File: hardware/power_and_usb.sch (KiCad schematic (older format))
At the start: 17 parts

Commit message: Finished routing USB type-c and battery charging IC
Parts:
- added C?: 10uF 25V, symbol Device:C
- added C?: 4.7uF, symbol Device:C
- added C?: 47nF, symbol Device:C
- added C? (x2): 10uF, symbol Device:C
- added C?: 8.2uF, symbol Device:C
- added C?: 1uF, symbol Device:C
- added C? (x2): 100nF, symbol Device:C
- added D?: LED, symbol Device:LED
- added JP?: Jumper, symbol Jumper:Jumper_2_Open
- added L?: 1uF, symbol Device:L
- added Q?: SN7002NH6327, Package_TO_SOT_SMD:SOT-23, symbol Device:Q_NMOS_GDS
- added R? (x2): 5K1, symbol Device:R
- added R?: 2K2, symbol Device:R
- added R?: 260R, symbol Device:R
- added R?: 5.23K, symbol Device:R
- added R?: 30.1K, symbol Device:R
- added R? (x6): 10K, symbol Device:R
- added R? (x2): 0R, Resistor_SMD:R_1206_3216Metric, symbol Device:R
- added R?: 220R, symbol Device:R
- added TH?: Thermistor 10k, symbol Device:Thermistor
- BT?: value Battery_Cell -> Li-Po Battery; Battery Description (none) -> 1S 3.7V 5000mAh
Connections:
- net labels added: BQ25890_INT, BQ25890_SCL, BQ25890_SDA, CE, CH340_RX, CH340_TX, DC-DC_PWR, GNDREF, Q_BOOST, Q_DISABLE, REGN, USB_PWR_D+, VBUS
- wire segments 45 -> 109
- no-connect marks 0 -> 13
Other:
- note added: "3.5...4.5V"
- note added: "3.9...14V at 3A"
- note added: "Solder it after programming and debugging"
- note added: "With/Without battery selector"
- note added: "with\nbattery"
- note added: "without\nbattery"
- note removed: "???"
- note removed: "Solder it after everything"
- moved on the sheet: BT?

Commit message: Add cubemx project Changed MCU and PD scheme
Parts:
- removed BT?: Li-Po Battery, symbol Device:Battery_Cell
- removed C?: 10uF 25V, symbol Device:C
- removed C?: 4.7uF, symbol Device:C
- removed C?: 47nF, symbol Device:C
- removed C? (x2): 10uF, symbol Device:C
- removed C?: 8.2uF, symbol Device:C
- removed C?: 1uF, symbol Device:C
- removed C?: 100nF, symbol Device:C
- removed D?: LED, symbol Device:LED
- removed JP?: Jumper, symbol Jumper:Jumper_2_Open
- removed L?: 1uF, symbol Device:L
- removed Q?: SN7002NH6327, Package_TO_SOT_SMD:SOT-23, symbol Device:Q_NMOS_GDS
- removed R? (x2): 5K1, symbol Device:R
- removed R?: 2K2, symbol Device:R
- removed R?: 260R, symbol Device:R
- removed R?: 5.23K, symbol Device:R
- removed R?: 30.1K, symbol Device:R
- removed R? (x6): 10K, symbol Device:R
- removed R?: 220R, symbol Device:R
- removed TH?: Thermistor 10k, symbol Device:Thermistor
- removed U?: BQ25890RTWR, QFN50P400X400X80-25N, symbol Batery:BQ25890RTWR
- added C?: 0.1uF, symbol Device:C
- added R?: 330R, symbol Device:R
- added U?: FUSB302BMPX, Package_DFN_QFN:WQFN-14-1EP_2.5x2.5mm_P0.5mm_EP1.45x1.45mm, symbol Interface_USB:FUSB302BMPX
- added U?: TPD4E02B04DQA, Package_SON:USON-10_2.5x1.0mm_P0.5mm, symbol Power_Protection:TPD4E02B04DQA
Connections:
- net labels added: CC1, CC2
- net labels removed: BQ25890_INT, BQ25890_SCL, BQ25890_SDA, CE, GNDREF, Q_BOOST, Q_DISABLE, REGN
- wire segments 109 -> 60
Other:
- note added: "ESD protection"
- note removed: "3.5...4.5V"
- note removed: "3.9...14V at 3A"
- moved on the sheet: J?, R?

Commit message: Changed flash for esp8266 Added stm32 schematic
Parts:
- removed C?: 100nF, symbol Device:C
- removed U?: CH340E, Package_SO:MSOP-10_3x3mm_P0.5mm, symbol Interface_USB:CH340E
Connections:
- net labels removed: CH340_RX, CH340_TX
- wire segments 60 -> 59
- no-connect marks 13 -> 10
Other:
- note removed: "USB-UART"
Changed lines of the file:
@@
 	4500 1150 5050 1150
-$Comp
-L Interface_USB:CH340E U?
-U 1 1 603B0049
-P 6450 5450
-F 0 "U?" H 6200 6000 50  0000 C CNN
-F 1 "CH340E" H 6650 4850 50  0000 C CNN
-F 2 "Package_SO:MSOP-10_3x3mm_P0.5mm" H 6500 4900 50  0001 L CNN
-F 3 "https://www.mpja.com/download/35227cpdata.pdf" H 6100 6250 50  0001 C CNN
-	1    6450 5450
-	1    0    0    -1
-$EndComp
-$Comp
-L power:GND #PWR?
-U 1 1 603B004F
-P 6450 6050
-F 0 "#PWR?" H 6450 5800 50  0001 C CNN
-F 1 "GND" H 6455 5877 50  0000 C CNN
-F 2 "" H 6450 6050 50  0001 C CNN
-F 3 "" H 6450 6050 50  0001 C CNN
-	1    6450 6050
-	1    0    0    -1
-$EndComp
-Text Notes 5950 6050 0    50   ~ 0
-USB-UART
 $Comp
 L Type-C:105450-0101 J?
@@
 Wire Notes Line
 	-700 5850 -2700 5850
-Text Label 6050 5450 2    50   ~ 0
-USB_UART_D-
-Text Label 6050 5350 2    50   ~ 0
-USB_UART_D+
 NoConn ~ 1050 7100
 NoConn ~ 1050 7000
@@
 Wire Notes Line
 	-700 3800 -2700 3800
-$Comp
-L power:+3.3V #PWR?
-U 1 1 6052E7D8
-P 6350 4850
-F 0 "#PWR?" H 6350 4700 50  0001 C CNN
-F 1 "+3.3V" H 6365 5023 50  0000 C CNN
-F 2 "" H 6350 4850 50  0001 C CNN
-F 3 "" H 6350 4850 50  0001 C CNN
-	1    6350 4850
-	1    0    0    -1
-$EndComp
-Wire Wire Line
-	6450 4850 6350 4850
-Connection ~ 6350 4850
-Text HLabel 6850 5050 2    50   Output ~ 0
-CH340_TX
-Text HLabel 6850 5150 2    50   Input ~ 0
-CH340_RX
-NoConn ~ 6850 5850
-NoConn ~ 6850 5350
-NoConn ~ 6050 5550
 Text Label 4300 2000 0    50   ~ 0
 DC-DC_PWR
-$Comp
-L Device:C C?
-U 1 1 6053E82B
-P 7300 5650
-F 0 "C?" H 7415 5696 50  0000 L CNN
-F 1 "100nF" H 7415 5605 50  0000 L CNN
-F 2 "" H 7338 5500 50  0001 C CNN
-F 3 "~" H 7300 5650 50  0001 C CNN
-	1    7300 5650
-	1    0    0    -1
-$EndComp
-$Comp
-L power:+3.3V #PWR?
-U 1 1 605408B8
-P 7300 5500
-F 0 "#PWR?" H 7300 5350 50  0001 C CNN
-F 1 "+3.3V" H 7315 5673 50  0000 C CNN
-F 2 "" H 7300 5500 50  0001 C CNN
-F 3 "" H 7300 5500 50  0001 C CNN
-	1    7300 5500
-	1    0    0    -1
-$EndComp
-$Comp
-L power:GND #PWR?
-U 1 1 6054128D
-P 7300 5800
-F 0 "#PWR?" H 7300 5550 50  0001 C CNN
-F 1 "GND" H 7305 5627 50  0000 C CNN
-F 2 "" H 7300 5800 50  0001 C CNN
-F 3 "" H 7300 5800 50  0001 C CNN
-	1    7300 5800
-	1    0    0    -1
-$EndComp
 Text Notes -3950 4050 0    50   ~ 0
 without\nbattery

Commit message: Changing power circuit again
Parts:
- removed JP? (x2): Jumper, symbol Jumper:Jumper_3_Open
- removed R? (x2): 0R, symbol Device:R
- removed R? (x2): 0R, Resistor_SMD:R_1206_3216Metric, symbol Device:R
- removed U?: FUSB302BMPX, Package_DFN_QFN:WQFN-14-1EP_2.5x2.5mm_P0.5mm_EP1.45x1.45mm, symbol Interface_USB:FUSB302BMPX
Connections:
- net labels removed: USB_PWR_D+, USB_PWR_D-, USB_UART_D+, USB_UART_D-, VCC
- wire segments 59 -> 54
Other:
- note removed: "Solder it after programming and debugging"
- note removed: "Use it during programming"
- note removed: "With/Without battery selector"
- note removed: "do NOT use BOTH top and bottom schematics"
- note removed: "with\nbattery"
- note removed: "without\nbattery"
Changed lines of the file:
@@
 Text Notes 1250 7500 0    50   ~ 0
 Type-C header
-$Comp
-L Jumper:Jumper_3_Open JP?
-U 1 1 603B9872
-P -2400 4350
-F 0 "JP?" V -2446 4437 50  0000 L CNN
-F 1 "Jumper" V -2355 4437 50  0000 L CNN
-F 2 "" H -2400 4350 50  0001 C CNN
-F 3 "~" H -2400 4350 50  0001 C CNN
-	1    -2400 4350
-	0    1    1    0
-$EndComp
-$Comp
-L Jumper:Jumper_3_Open JP?
-U 1 1 603BC5B8
-P -1500 4350
-F 0 "JP?" V -1546 4437 50  0000 L CNN
-F 1 "Jumper" V -1455 4437 50  0000 L CNN
-F 2 "" H -1500 4350 50  0001 C CNN
-F 3 "~" H -1500 4350 50  0001 C CNN
-	1    -1500 4350
-	0    1    1    0
-$EndComp
 Text Label 2450 6600 0    50   ~ 0
 D+
@@
 Text Label 2450 6700 0    50   ~ 0
 D-
-Text Label -2550 4350 0    50   ~ 0
-D+
-Text Label -1650 4350 0    50   ~ 0
-D-
-Text Label -2400 4100 0    50   ~ 0
-USB_UART_D+
-Text Label -1500 4100 0    50   ~ 0
-USB_UART_D-
-Text Label -1400 4600 0    50   ~ 0
-USB_PWR_D-
-Text Label -2300 4600 0    50   ~ 0
-USB_PWR_D+
-Wire Wire Line
-	-1500 4600 -1400 4600
-Wire Wire Line
-	-2400 4600 -2300 4600
-$Comp
-L Device:R R?
-U 1 1 603C2BE1
-P -1950 5200
-F 0 "R?" V -2157 5200 50  0000 C CNN
-F 1 "0R" V -2066 5200 50  0000 C CNN
-F 2 "" V -2020 5200 50  0001 C CNN
-F 3 "~" H -1950 5200 50  0001 C CNN
-	1    -1950 5200
-	0    1    1    0
-$EndComp
-$Comp
-L Device:R R?
-U 1 1 603C3C5A
-P -1950 5600
-F 0 "R?" V -2157 5600 50  0000 C CNN
-F 1 "0R" V -2066 5600 50  0000 C CNN
-F 2 "" V -2020 5600 50  0001 C CNN
-F 3 "~" H -1950 5600 50  0001 C CNN
-	1    -1950 5600
-	0    1    1    0
-$EndComp
-Text Label -1800 5200 0    50   ~ 0
-USB_PWR_D+
-Text Label -1800 5600 0    50   ~ 0
-USB_PWR_D-
-Text Label -2100 5600 2    50   ~ 0
-D-
-Text Label -2100 5200 2    50   ~ 0
-D+
-Wire Notes Line
-	-2600 4700 -850 4700
-Wire Notes Line
-	-850 4700 -850 4000
-Wire Notes Line
-	-850 4000 -2600 4000
-Wire Notes Line
-	-2600 4000 -2600 4700
-Wire Notes Line
-	-2250 4950 -2250 5700
-Wire Notes Line
-	-2250 5700 -1250 5700
-Wire Notes Line
-	-1250 5700 -1250 4950
-Wire Notes Line
-	-1250 4950 -2250 4950
-Text Notes -2250 3950 0    50   ~ 0
-Use it during programming
-Text Notes -2550 5800 0    50   ~ 0
-Solder it after programming and debugging
-Text Notes -2650 4850 0    50   ~ 0
-do NOT use BOTH top and bottom schematics
-Wire Notes Line
-	-2700 5850 -2700 3800
-Wire Notes Line
-	-700 5850 -2700 5850
 NoConn ~ 1050 7100
 NoConn ~ 1050 7000
@@
 Text Label 700  850  0    50   ~ 0
 DC-DC_PWR
-$Comp
-L Device:R R?
-U 1 1 6045FB2F
-P -4100 4150
-F 0 "R?" V -4307 4150 50  0000 C CNN
-F 1 "0R" V -4216 4150 50  0000 C CNN
-F 2 "Resistor_SMD:R_1206_3216Metric" V -4170 4150 50  0001 C CNN
-F 3 "~" H -4100 4150 50  0001 C CNN
-	1    -4100 4150
-	0    1    1    0
-$EndComp
-$Comp
-L Device:R R?
-U 1 1 604601EF
-P -4100 4550
-F 0 "R?" V -4307 4550 50  0000 C CNN
-F 1 "0R" V -4216 4550 50  0000 C CNN
-F 2 "Resistor_SMD:R_1206_3216Metric" V -4170 4550 50  0001 C CNN
-F 3 "~" H -4100 4550 50  0001 C CNN
-	1    -4100 4550
-	0    1    1    0
-$EndComp
-Text Label -3950 4150 0    50   ~ 0
-DC-DC_PWR
-Text Label -3950 4550 0    50   ~ 0
-DC-DC_PWR
-$Comp
-L power:VBUS #PWR?
-U 1 1 60465C61
-P -4400 4150
-F 0 "#PWR?" H -4400 4000 50  0001 C CNN
-F 1 "VBUS" H -4385 4323 50  0000 C CNN
-F 2 "" H -4400 4150 50  0001 C CNN
-F 3 "" H -4400 4150 50  0001 C CNN
-	1    -4400 4150
-	1    0    0    -1
-$EndComp
-$Comp
-L power:VCC #PWR?
-U 1 1 60466B91
-P -4400 4550
-F 0 "#PWR?" H -4400 4400 50  0001 C CNN
-F 1 "VCC" H -4385 4723 50  0000 C CNN
-F 2 "" H -4400 4550 50  0001 C CNN
-F 3 "" H -4400 4550 50  0001 C CNN
-	1    -4400 4550
-	1    0    0    -1
-$EndComp
-Wire Wire Line
-	-4400 4550 -4250 4550
-Wire Wire Line
-	-4400 4150 -4250 4150
-Wire Notes Line
-	-4550 4650 -3450 4650
-Wire Notes Line
-	-3450 4650 -3450 3850
-Wire Notes Line
-	-3450 3850 -4550 3850
-Wire Notes Line
-	-4550 3850 -4550 4650
-Text Notes -4550 3800 0    50   ~ 0
-With/Without battery selector
-Wire Notes Line
-	-700 5850 -700 3800
-Wire Notes Line
-	-700 3800 -2700 3800
 Text Label 4300 2000 0    50   ~ 0
 DC-DC_PWR
-Text Notes -3950 4050 0    50   ~ 0
-without\nbattery
-Text Notes -3950 4450 0    50   ~ 0
-with\nbattery
-$Comp
-L power:VBUS #PWR?
-U 1 1 603EA1A9
-P 9900 5450
-F 0 "#PWR?" H 9900 5300 50  0001 C CNN
-F 1 "VBUS" H 9915 5623 50  0000 C CNN
-F 2 "" H 9900 5450 50  0001 C CNN
-F 3 "" H 9900 5450 50  0001 C CNN
-	1    9900 5450
-	1    0    0    -1
-$EndComp
-Wire Wire Line
-	9900 5450 9800 5450
-$Comp
-L Interface_USB:FUSB302BMPX U?
-U 1 1 603EFB15
-P 9300 5550
-F 0 "U?" H 9300 5061 50  0000 C CNN
-F 1 "FUSB302BMPX" H 9300 4970 50  0000 C CNN
-F 2 "Package_DFN_QFN:WQFN-14-1EP_2.5x2.5mm_P0.5mm_EP1.45x1.45mm" H 9300 5050 50  0001 C CNN
-F 3 "http://www.onsemi.com/pub/Collateral/FUSB302B-D.PDF" H 9400 5150 50  0001 C CNN
-	1    9300 5550
-	1    0    0    -1
-$EndComp
 Text Label 1050 6400 2    50   ~ 0
 CC2

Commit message: Finished power schematics
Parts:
- removed C?: 10uF 25V, symbol Device:C
- removed C?: 3.3nF, symbol Device:C
- removed C?: 100nF, symbol Device:C
- removed C?: 22uF, symbol Device:C
- removed L?: 2.2uH, symbol Device:L
- removed R? (x2): 100K, symbol Device:R
- removed R?: 316K, symbol Device:R
- removed U?: TPS62150RGTR, QFN50P300X300X100-17N, symbol TSP62150:TPS62150RGTR
- added BT?: Li-Po Battery, symbol Device:Battery_Cell
- added C? (x3): 100nF, symbol Device:C
- added C?: 10uF 25V, symbol Device:C
- added C?: 4.7uF, symbol Device:C
- added C?: 47nF, symbol Device:C
- added C? (x3): 10uF, symbol Device:C
- added C? (x4): 1uF, symbol Device:C
- added C? (x2): 470pF, symbol Device:C
- added D?: TS3USB221DCDR, Package_SON:VSON-10-1EP_3x3mm_P0.5mm_EP1.65x2.4mm_ThermalVias, symbol ts3usb221dcdr:TS3USB221DCDR
- added D?: LED, symbol Device:LED
- added L?: 2.2uH, symbol Device:L
- added R? (x4): 4K7, symbol Device:R
- added R?: 2K2, symbol Device:R
- added R?: 260R, symbol Device:R
- added R?: 5K23, symbol Device:R
- added R?: 30K1, symbol Device:R
- added R? (x5): 10K, symbol Device:R
- added R? (x3): 0R, symbol Device:R
- added R? (x2): 5K1, symbol Device:R
- added R?: 200R, symbol Device:R
- added SW?: Button, symbol Switch:SW_Push
- added TH?: Thermistor 10K, symbol Device:Thermistor
- added U?: BQ25895RTW, Package_DFN_QFN:Texas_S-PWQFN-N24_EP2.7x2.7mm_ThermalVias, symbol Battery_Management:BQ25895RTW
- added U?: TLV75533PDBV, Package_TO_SOT_SMD:SOT-23-5, symbol Regulator_Linear:TLV75533PDBV
- added U?: FUSB302BMPX, Package_DFN_QFN:WQFN-14-1EP_2.5x2.5mm_P0.5mm_EP1.45x1.45mm, symbol Interface_USB:FUSB302BMPX
- C?: value 0.1uF -> 100nF
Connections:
- net labels added: BQ25895_INT, BQ25895_SCL, BQ25895_SDA, ChargeEnable, ControlSelect, FUSB302_INT, FUSB302_SCL, FUSB302_SDA, GNDA, GNDPWR, USB_D+, USB_D-, USB_PWR_D+, USB_PWR_D-, VCC
- net labels removed: DC-DC_PWR, FB, VOS
- wire segments 54 -> 127
- no-connect marks 10 -> 11
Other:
- note added: "+5V"
- note added: "3.5...4.75V"
- note added: "3.9...14V at 3A"
- note added: "500mA"
- note added: "Battery Thermistor"
- note added: "Full reset"
- note added: "If without battery, place R \ninstead of TS3USB221"
- note added: "If without battery,\nplace R \ninstead of FUSB302"
- note added: "WITHOUT\nBATTERY\nJUMPER"
- note added: "Without battery:\n- no bq25895\n- no fusb302mpx, R on CC pins instead\n- TLV75533 jumper\n"
- note removed: "3.3...17V"
- note removed: "AVIN - AGND\ncapacitor"
- moved on the sheet: C?, J?, R?, U?

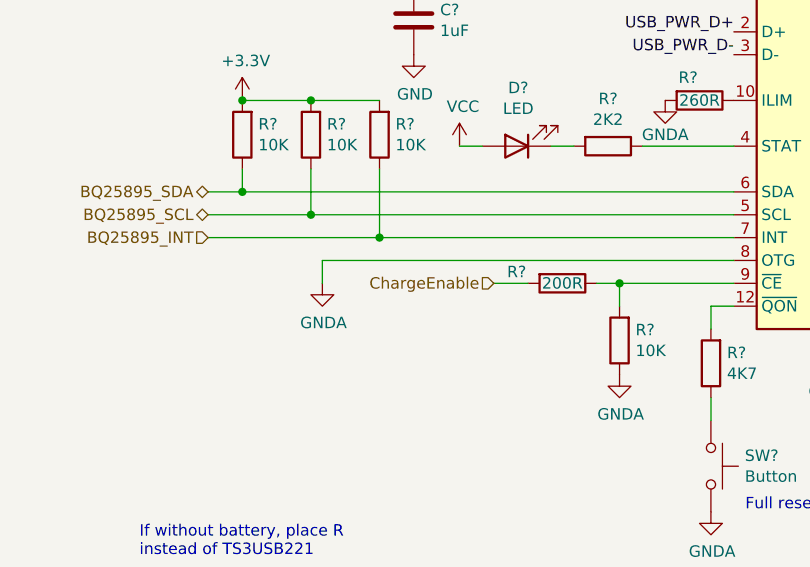
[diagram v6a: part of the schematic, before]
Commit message: Finished sx1278 schematic
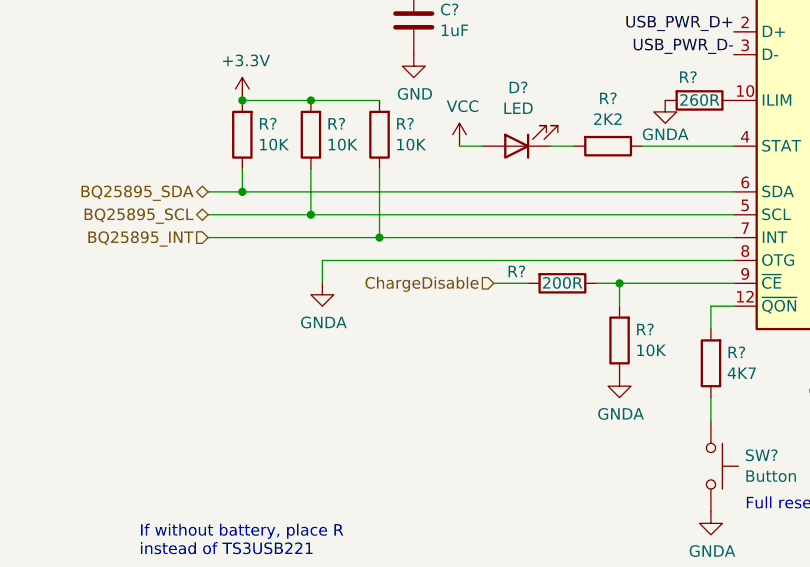
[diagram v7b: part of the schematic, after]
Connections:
- net ChargeEnable renamed ChargeDisable
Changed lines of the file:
@@
 	8100 3500 8850 3500
 Text HLabel 6250 4600 0    50   Input ~ 0
-ChargeEnable
+ChargeDisable
 Text Label 8500 4400 0    50   ~ 0
 ControlSelect

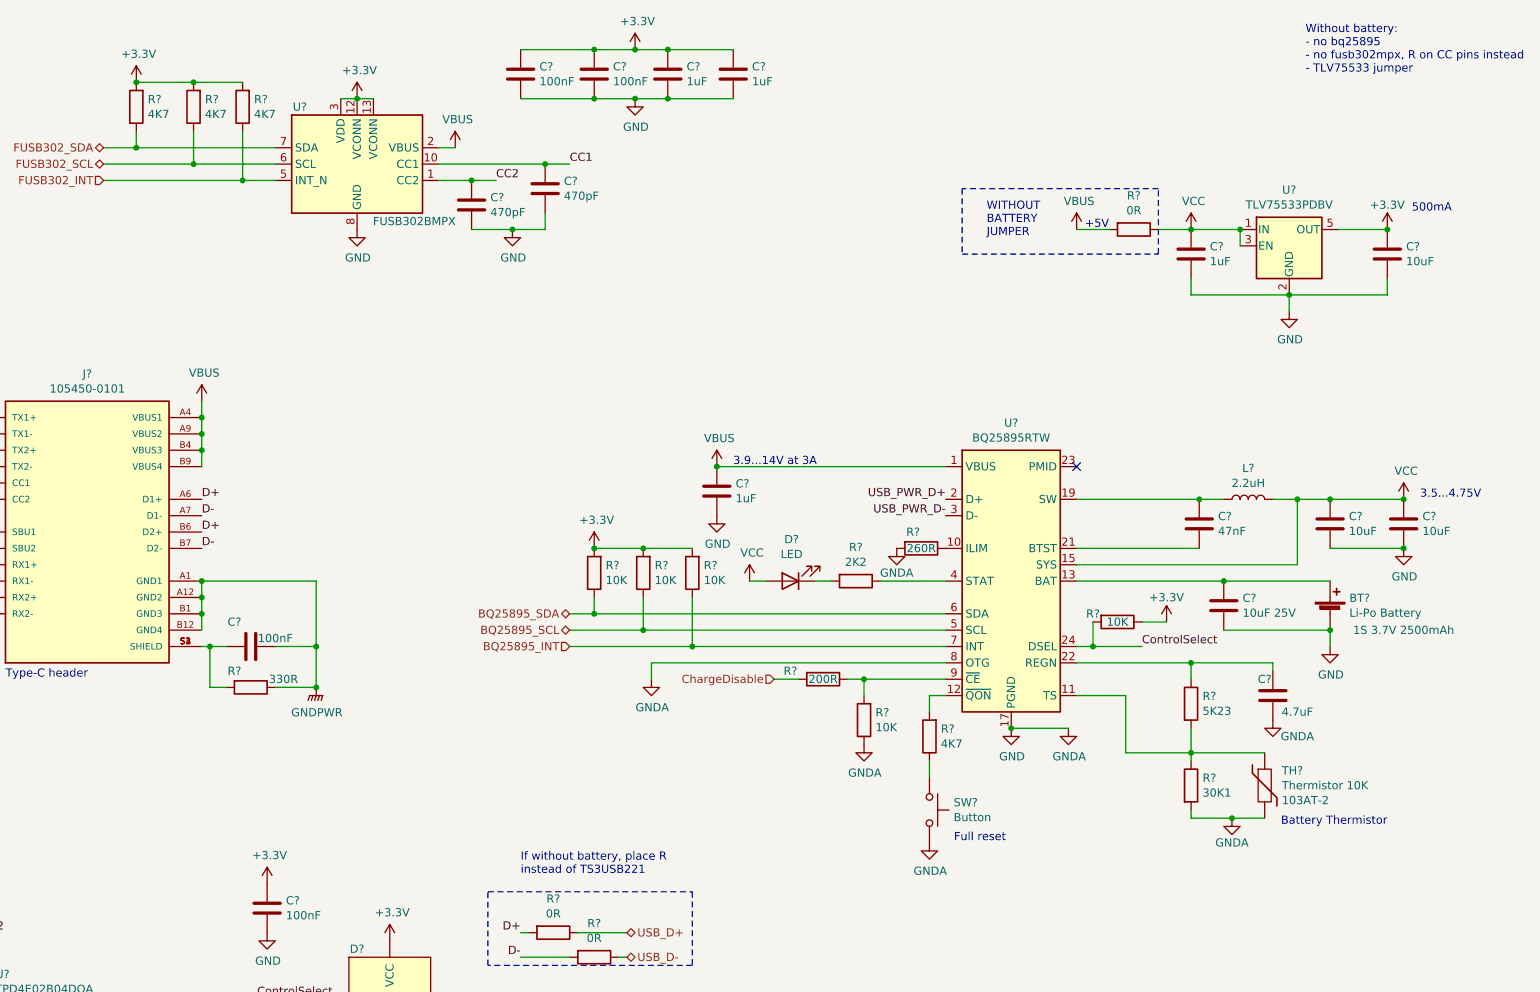
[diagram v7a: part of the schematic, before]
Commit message: Select crystals, add HSE for stm32 and fixed some bits
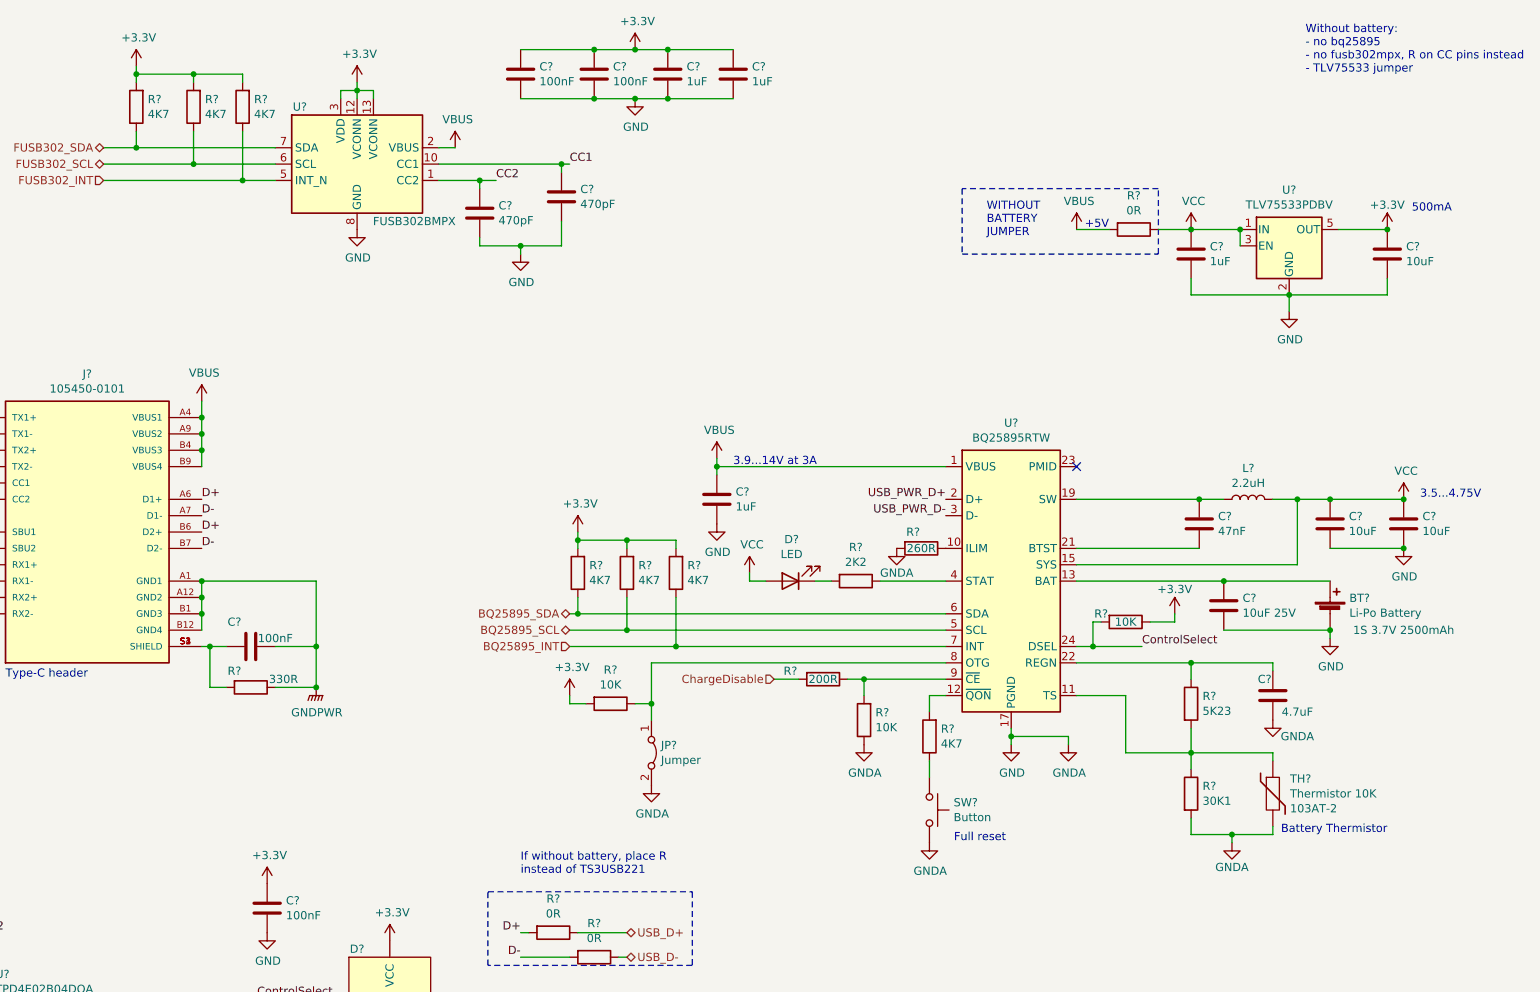
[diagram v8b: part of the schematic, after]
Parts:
- added JP?: Jumper, symbol Jumper:Jumper_2_Bridged
- added R?: 10K, symbol Device:R
- R? (x3): value 10K -> 4K7
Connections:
- net +3V3: now also R?.2
- net GND: now also JP?.2 (B); no longer U?.8 (OTG)
- new net: JP?.1 (A), R?.1, U?.8 (OTG)
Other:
- moved on the sheet: C?, R?, TH?
